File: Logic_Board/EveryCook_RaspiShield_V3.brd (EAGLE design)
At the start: 96.2 x 61.4 mm, 95 parts, among them IC1 TLP281-4, IC2 TLP281-4, J1 6P-2.54mm, J4 6P-2.54mm, J5 JUMPERSMD, Q2 IRLZ44N, U1 AD7794BRUZ, U2 PCA9685PW, U4 78M05, U7 CJ1117-3.3

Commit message: Schematic of logic board finished, only audio amp missing. Board ripped up for redraw
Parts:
- removed C4: 100uF/16V, Discrete:ELECTRO-SMD-C-6MM
- removed C8: 0.1uF, Discrete:0603
- removed D3: M7, Discrete:D2010
- removed IC1: TLP281-4, IC:SO16
- removed J1: 6P-2.54mm, Connector:6P-2.54-80/40MIL
- removed J14: (no value), Connector:2P-5.0
- removed J4: 6P-2.54mm, Connector:6P-2.54-65/35MIL
- removed J5: JUMPERSMD, Discrete:2P-JUMPER
- removed L2: 47uH, Discrete:0630
- removed R1, R10, R11, R12, R13, R18, R19, R20, R21, R26, R27, R28, R29, R6, R7, R8, R9: 1k, Discrete:0603
- removed R14: 51k, Discrete:0603
- removed R15, R22, R23, R24, R25: 10k, Discrete:0603
- removed R16: 2k, Discrete:0603
- removed R5: 4.7k, Discrete:0603
- removed U$2: LM2596, IC:TO-263
- removed U13, U14, U15, U16, U17: (no value), Connector:RJ45-N
- removed U2: PCA9685PW, wia:SOP65P640X110-28N
- added BUT1, BUT2, BUT3, C_CLOSE, C_LOCK, FAN, I2C, P_LOCK, THSTAT_POT: (no value), pinhead:1X02
- added C14: 22pF, Discrete:0603
- added C15: 0.1uF, Discrete:0603
- added DISPLAY, POWR_BRD: (no value), pinhead:2X06
- added Q1: 8 MHz, crystal:HC49UP
- added Q3: BSP372, infineon:PG-SOT-223
- added R3, R40, R45, R46: 10k, Discrete:0603
- added R39, R4, R44, R47, R48: 1k, Discrete:0603
- added T2: (no value), zetex:SM8
- added VALVE+PROXSW: (no value), pinhead:1X04
- added X1, X2, X3, X4, X5: MINI-USB_4P-85-32006-601-1, con-cypressindustries:85-32006-601-1
- C3: value 220uF/35V -> 22pF; device Discrete:ELECTRO-SMD-G-10MM -> Discrete:0603
- IC2: value TLP281-4 -> ATMEGA644A; device IC:SO16 -> atmel:TQFP44
- Q2: value IRLZ44N -> BSP372; device Discrete:D2PAK -> infineon:PG-SOT-223
- moved Q2 151.8 mm to (-64.8, -18.5), turned to 0 degrees
- moved C3 106.3 mm to (2.29, 80.1), turned to 0 degrees
- moved IC2 55.8 mm to (58.9, 71.8), turned to 0 degrees
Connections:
- removed net +24V: C2.+, C3.+, J2.2, U$2.1, U4.1
- removed net 3V3: C10.2, C17.2, C18.2, C6.+, C9.2, IC1.10, IC1.12, IC1.14, IC1.16, R26.2, R27.2, R28.2, R29.2, U1.22, U16.2, U16.6, U16.8, U17.10, U17.9, U2.28, U7.2, U7.4
- removed net BUTTON: IC2.11, IC2.13, IC2.15, IC2.9, J4.2
- removed net CS: U$1.24, U1.3
- removed net D5V: C1.+, C4.+, C8.2, J5.2, L2.P$2, U$2.4, U15.6, U7.3
- removed net GPIO1: R41.2, U$1.11, U16.1
- removed net GPIO2: R42.2, U$1.13, U16.3
- removed net KEY1: IC2.16, R5.1
- removed net KEY1S: IC2.2, U$1.12
- removed net KEY2: IC2.14, R14.1
- removed net KEY2S: IC2.4, U$1.16
- removed net KEY3: IC2.12, R15.1
- removed net KEY3S: IC2.6, U$1.18
- removed net KEY4: IC2.10, R16.1
- removed net KEY4S: IC2.8, U$1.22
- removed net LED: IC1.2, J4.3
- removed net LED-1: R6.2, U17.1
- removed net LED-2: R7.2, U17.2
- removed net LED-3: R8.2, U17.3
- removed net LED-4: R9.2, U17.4
- removed net LED-5: R10.2, U17.5
- removed net LED-6: R11.2, U17.6
- removed net LED-7: R12.2, U17.7
- removed net LED-8: R13.1, U17.8
- removed net LED1: IC1.4, J4.4
- removed net LED1S: IC1.13, R23.2, U$1.8
- removed net LED2: IC1.6, J4.5
- removed net LED2S: IC1.11, R24.2, U$1.10
- removed net LED3: IC1.8, J4.6
- removed net LED3S: IC1.9, R25.2, U$1.26
- removed net LEDS: IC1.15, R22.2, U$1.7
- removed net MVCC: J14.1, J3.1
- removed net N$13: R1.2, U2.6
- removed net N$14: J1.2, U2.18
- removed net N$20: IC1.1, R18.1
- removed net N$21: IC1.3, R19.1
- removed net N$22: IC1.5, R20.1
- removed net N$23: IC1.7, R21.1
- removed net N$25: R6.1, U2.8
- removed net N$26: R7.1, U2.9
- removed net N$27: R8.1, U2.10
- removed net N$28: R9.1, U2.11
- removed net N$29: R10.1, U2.12
- removed net N$3: Q2.1, R1.1
- removed net N$30: R11.1, U2.13
- removed net N$31: R12.1, U2.15
- removed net N$32: R13.2, U2.16
- removed net N$33: J1.3, U2.19
- removed net N$34: J1.4, U2.20
- removed net N$35: J1.5, U2.21
- removed net N$36: J1.6, U2.22
- removed net N$4: J1.1, U2.17
- removed net N$67: IC2.1, R26.1
- removed net N$68: IC2.3, R27.1
- removed net N$69: IC2.5, R28.1
- removed net N$70: IC2.7, R29.1
- removed net N$91: U15.7
- removed net SCL: U$1.5, U2.26
- removed net SDA: U$1.3, U2.27
- removed net SERVO_SIG: U15.8, U2.7
- new net +12V: C2.+, FAN.1, J3.1, U4.1, VALVE+PROXSW.1
- new net +3V3: C10.2, C15.2, C17.2, C18.2, C6.+, C9.2, IC2.38, IC2.5, POWR_BRD.4, R3.2, R45.1, U1.22, U7.2
- new net +5V: C1.+, J2.2, R46.2, T2.1, U7.3
- new net AVCC: IC2.27
- new net DAEMON_RST_LINE: IC2.19, R44.1
- new net FAN_PWM: Q2.1, R4.1
- new net IH_OFF: IC2.11, POWR_BRD.9
- new net IH_ON: POWR_BRD.5
- new net IH_PWR: IC2.15, POWR_BRD.1
- new net IH_RUN: IC2.12, POWR_BRD.7
- new net IH_THERMISTOR: IC2.36, POWR_BRD.2, R40.2
- new net MOT_PWM: IC2.14, POWR_BRD.3
- new net N$10: IC2.16, R4.2
- new net N$11: DISPLAY.12, IC2.21
- new net N$12: I2C.2, U$1.3
- new net N$15: DISPLAY.11, IC2.22
- new net N$16: DISPLAY.10, IC2.23
- new net N$17: DISPLAY.9, IC2.24
- new net N$18: DISPLAY.8, IC2.25
- new net N$19: DISPLAY.7, IC2.26
- new net N$37: DISPLAY.6, IC2.40
- new net N$38: DISPLAY.5, IC2.41
- new net N$39: DISPLAY.4, IC2.42
- new net N$41: DISPLAY.3, IC2.43
- new net N$43: DISPLAY.1, IC2.44
- new net N$49: DISPLAY.2, IC2.37
- new net N$50: I2C.1, U$1.5
- new net N$51: FAN.2, Q2.2
- new net N$52: IC2.9, U$1.8
- new net N$54: IC2.10, U$1.10
- new net N$55: IC2.2, U$1.16
- new net N$56: IC2.1, U$1.12
- new net N$59: C_CLOSE.1, IC2.30
- new net N$6: IC2.4, R3.1
- new net N$60: C_LOCK.1, IC2.31
- new net N$61: IC2.32, P_LOCK.1
- new net N$62: BUT2.1
- new net N$63: BUT3.1
- new net N$64: R39.2
- new net N$66: BUT1.1, R39.1, R44.2, R45.2
- new net N$7: C14.1, IC2.8, Q1.1
- new net N$71: R47.2, T2.4
- new net N$72: R46.1, T2.2, T2.5
- new net N$77: Q3.2, VALVE+PROXSW.2
- new net N$8: IC2.3, U$1.18
- new net PROX_SWI: IC2.35, VALVE+PROXSW.3
- new net RPI_RST: IC2.20, R47.1
- new net SAFETY_CHAIN: IC2.33
- new net VALVE_OPEN: Q3.1, R48.1
- net GND: now also BUT1.2, BUT2.2, BUT3.2, C14.2, C15.1, C3.2, C_CLOSE.2, C_LOCK.2, IC2.39, IC2.6, P_LOCK.2, Q2.3, Q3.3, R40.1, T2.3, THSTAT_POT.2, U1.3, VALVE+PROXSW.4, X1.4, X2.4, X3.4, X4.4, X5.4; no longer C3.-, C4.-, C8.1, D3.+, R22.1, R23.1, R24.1, R25.1, U$2.3, U$2.5, U13.3, U13.4, U14.3, U14.4, U15.3, U15.4, U16.5, U2.1, U2.14, U2.2, U2.23, U2.24, U2.25, U2.3, U2.4, U2.5, U4.3
- net GPIO3: no longer U$1.15, U16.7
- net L5V: now also X1.1, X2.1, X3.1, X4.1, X5.1; no longer U13.5, U13.6, U14.5, U14.6, U15.5
- net LOADCELL1_SIG+: now also X2.2; no longer U13.7
- net LOADCELL1_SIG-: now also X2.3; no longer U13.8
- net LOADCELL2_SIG+: now also X1.2; no longer U13.1
- net LOADCELL2_SIG-: now also X1.3; no longer U13.2
- net LOADCELL3_SIG+: now also X4.2; no longer U14.7
- net LOADCELL3_SIG-: now also X4.3; no longer U14.8
- net LOADCELL4_SIG+: now also X3.2; no longer U14.1
- net LOADCELL4_SIG-: now also X3.3; no longer U14.2
- net N$2: now also C3.1, IC2.7, Q1.2; no longer J14.2, Q2.2
- net N$58: now also T2.8; no longer J5.1
- net N$65: now also IC2.34, R48.2; no longer D3.-, L2.P$1, U$2.2
- net PGND: now also IC2.18, IC2.28; no longer Q2.3, U13.10, U13.9, U14.10, U14.9, U15.10, U15.9, U16.10, U16.9
- net PRESS_SIG+: now also X5.2; no longer U15.1
- net PRESS_SIG-: now also X5.3; no longer U15.2
- net TEMPER_SIG+: now also THSTAT_POT.1; no longer U16.4
- net VCC: now also IC2.17; no longer J4.1, R14.2, R15.2, R16.2, R18.2, R19.2, R20.2, R21.2, R5.2
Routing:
- net 3V3: track 184.8 -> 0.00 mm, vias 6 -> 0
- net PGND: track 169.9 -> 0.00 mm, vias 1 -> 0
- net L5V: track 160.6 -> 9.59 mm, vias 3 -> 0
- net D5V: track 102.3 -> 0.00 mm, vias 1 -> 0
- net LED-1: track 82.3 -> 0.00 mm, vias 2 -> 0
- net +24V: track 80.5 -> 0.00 mm
- net GPIO3: track 74.7 -> 0.00 mm, vias 1 -> 0
- net GPIO2: track 73.9 -> 0.00 mm, vias 1 -> 0
- net GPIO1: track 72.4 -> 0.00 mm, vias 1 -> 0
- net LED-8: track 70.5 -> 0.00 mm, vias 1 -> 0
- net LED-7: track 70.4 -> 0.00 mm, vias 1 -> 0
- net SERVO_SIG: track 66.9 -> 0.00 mm, vias 4 -> 0
- net LED-5: track 63.3 -> 0.00 mm, vias 2 -> 0
- net LED-2: track 59.3 -> 0.00 mm, vias 2 -> 0
- net LED-4: track 58.1 -> 0.00 mm, vias 1 -> 0
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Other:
- board text removed: "Total Cost: around 60RMB"

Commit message: Logic board all routed...
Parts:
- removed R41, R42, R43: 10k, Discrete:0603
- removed THSTAT_POT: (no value), pinhead:1X02
- removed U$1: RASPBERRY-PI, RaspberryPi:RASPBERRY-PI
- removed X1, X2, X3, X4, X5: MINI-USB_4P-85-32006-601-1, con-cypressindustries:85-32006-601-1
- added AIN_GND, AIN_SIG: (no value), wirepad:2,15/1,0
- added C16, C8: 10uF, Discrete:0603
- added C38: 100uF/25V, Discrete:ELECTRO-SMD-B-4.8MM
- added C4: 220pF, Discrete:0603
- added IC1: LM386MM-1, linear:MMSOP08
- added LC1, LC2, LC3, LC4, PRESS: MINI-USB_4P-85-32006-601-1, con-cypressindustries:85-32006-601-1
- added R1, R5: 5k, Discrete:0603
- added R6, R7: 10k, Discrete:0603
- added RASPI_CONNECTOR_(TOP): (no value), pinhead:2X13
- added SP1: AL23P, buzzer:AL23P
- added TEMP: (no value), pinhead:1X02
- R3: value 10k -> 22k
- T2: value (none) -> ZDT6790
- moved VALVE+PROXSW 359.0 mm to (89.5, 78.3)
- moved R48 320.6 mm to (66.2, 49.7), turned to 180 degrees
- moved Q3 317.5 mm to (76.7, 47.1), turned to 180 degrees
- moved R46 232.9 mm to (90.2, 52.2)
- moved T2 228.2 mm to (94.8, 48.0), turned to 270 degrees
- moved R47 227.3 mm to (90.5, 41.5), turned to 90 degrees
- moved R45 225.9 mm to (92.3, 66.2), turned to 90 degrees
- moved R39 223.7 mm to (94.4, 66.2), turned to 270 degrees
- moved R44 223.1 mm to (90.9, 66.2), turned to 90 degrees
- moved BUT1 215.6 mm to (94.4, 70.5), turned to 90 degrees
- moved BUT2 215.1 mm to (88.4, 70.5), turned to 90 degrees
- moved BUT3 215.1 mm to (82.7, 70.5), turned to 90 degrees
- moved P_LOCK 203.3 mm to (75.9, 77.3), turned to 90 degrees
- moved C_LOCK 203.1 mm to (81.3, 77.3), turned to 90 degrees
- moved C_CLOSE 183.8 mm to (70.2, 77.2), turned to 90 degrees
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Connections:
- removed net AVCC: IC2.27
- removed net GPIO3: R43.2
- removed net N$40: U$1.19, U1.24
- removed net VCC: IC2.17
- new net MOSI: RASPI_CONNECTOR_(TOP).19, U1.24
- new net N$14: IC1.3, R1.2, R5.1
- new net N$22: C16.1, C38.+, IC1.5
- new net N$23: C38.-, SP1.1
- new net N$27: AIN_SIG.1, C4.2
- new net N$3: C4.1, R5.2
- net +3V3: now also IC2.17, IC2.27, R6.1, R7.1
- net +5V: now also C16.2, IC1.6
- net GND: now also AIN_GND.1, C8.1, IC1.2, IC1.4, IC2.18, IC2.28, LC1.4, LC2.4, LC3.4, LC4.4, PRESS.4, R1.1, RASPI_CONNECTOR_(TOP).6, SP1.2, TEMP.2; no longer R41.1, R42.1, R43.1, THSTAT_POT.2, U$1.6, X1.4, X2.4, X3.4, X4.4, X5.4
- net IH_ON: now also IC2.13
- net L5V: now also LC1.1, LC2.1, LC3.1, LC4.1, PRESS.1; no longer X1.1, X2.1, X3.1, X4.1, X5.1
- net LOADCELL1_SIG+: now also LC1.2; no longer X2.2
- net LOADCELL1_SIG-: now also LC1.3; no longer X2.3
- net LOADCELL2_SIG+: now also LC2.2; no longer X1.2
- net LOADCELL2_SIG-: now also LC2.3; no longer X1.3
- net LOADCELL3_SIG+: now also LC3.2; no longer X4.2
- net LOADCELL3_SIG-: now also LC3.3; no longer X4.3
- net LOADCELL4_SIG+: now also LC4.2; no longer X3.2
- net LOADCELL4_SIG-: now also LC4.3; no longer X3.3
- net MISO: now also RASPI_CONNECTOR_(TOP).21; no longer U$1.21
- net N$12: now also RASPI_CONNECTOR_(TOP).3; no longer U$1.3
- net N$50: now also RASPI_CONNECTOR_(TOP).5; no longer U$1.5
- net N$52: now also RASPI_CONNECTOR_(TOP).8; no longer U$1.8
- net N$54: now also RASPI_CONNECTOR_(TOP).10; no longer U$1.10
- net N$55: now also RASPI_CONNECTOR_(TOP).16; no longer U$1.16
- net N$56: now also RASPI_CONNECTOR_(TOP).12; no longer U$1.12
- net N$58: now also RASPI_CONNECTOR_(TOP).2; no longer U$1.2
- net N$6: now also C8.2, RASPI_CONNECTOR_(TOP).11
- net N$62: now also R7.2, RASPI_CONNECTOR_(TOP).24
- net N$63: now also R6.2, RASPI_CONNECTOR_(TOP).26
- net N$64: now also RASPI_CONNECTOR_(TOP).22
- net N$8: now also RASPI_CONNECTOR_(TOP).18; no longer U$1.18
- net PGND: no longer IC2.18, IC2.28
- net PRESS_SIG+: now also PRESS.2; no longer X5.2
- net PRESS_SIG-: now also PRESS.3; no longer X5.3
- net SAFETY_CHAIN: now also POWR_BRD.11
- net SCLK: now also RASPI_CONNECTOR_(TOP).23; no longer U$1.23
- net TEMPER_SIG+: now also TEMP.1; no longer THSTAT_POT.1
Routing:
- net GND: track 11.2 -> 691.4 mm, vias 0 -> 11
- net +3V3: track 11.7 -> 271.7 mm, vias 0 -> 21
- net +5V: track 1.91 -> 187.2 mm, vias 0 -> 4
- net L5V: track 9.59 -> 186.9 mm, vias 0 -> 9
- net PGND: track 0.00 -> 152.4 mm
- net +12V: track 0.00 -> 142.3 mm
- net N$54: track 0.00 -> 84.0 mm, vias 0 -> 8
- net N$55: track 0.00 -> 77.7 mm, vias 0 -> 6
- net N$6: track 0.00 -> 77.1 mm, vias 0 -> 3
- net N$11: track 0.00 -> 76.2 mm, vias 0 -> 6
- net DAEMON_RST_LINE: track 0.00 -> 75.2 mm, vias 0 -> 4
- net IH_PWR: track 0.00 -> 73.3 mm, vias 0 -> 4
- net N$56: track 0.00 -> 71.7 mm, vias 0 -> 4
- net IH_OFF: track 0.00 -> 66.4 mm, vias 0 -> 3
- net IH_ON: track 0.00 -> 65.7 mm, vias 0 -> 4
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- added copper zone on layer 16, net N$21
- added copper zone on layer 1, net N$28
- removed copper zone on layer 1, net GND
- removed copper zone on layer 16, net GND
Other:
- board size 96.2 x 61.4 mm -> 103.1 x 86.4 mm
- board text added: "0V"
- board text added: "12V"
- board text added: "EveryCook.org/opensource"
- board text added: "connect cable with 3.5mm 90° angle jack"
- board text added: "pGND"
- board text added: "speaker (bottom side)"
- board text removed: "Change later probably to GPIO"
- board text removed: "EveryCook"
- board text removed: "Induction Conn"

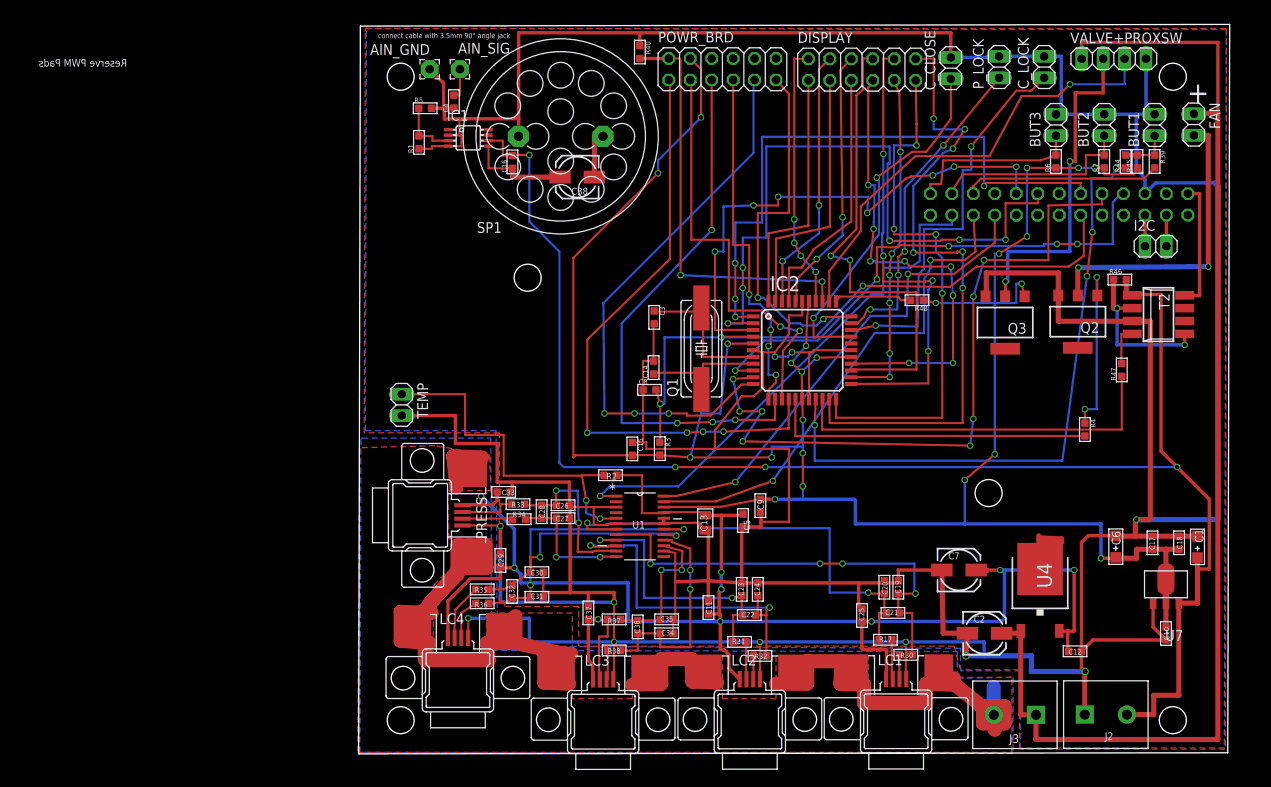
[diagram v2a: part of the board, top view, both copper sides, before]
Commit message: changed all 0606 to 0805 package for R and C.
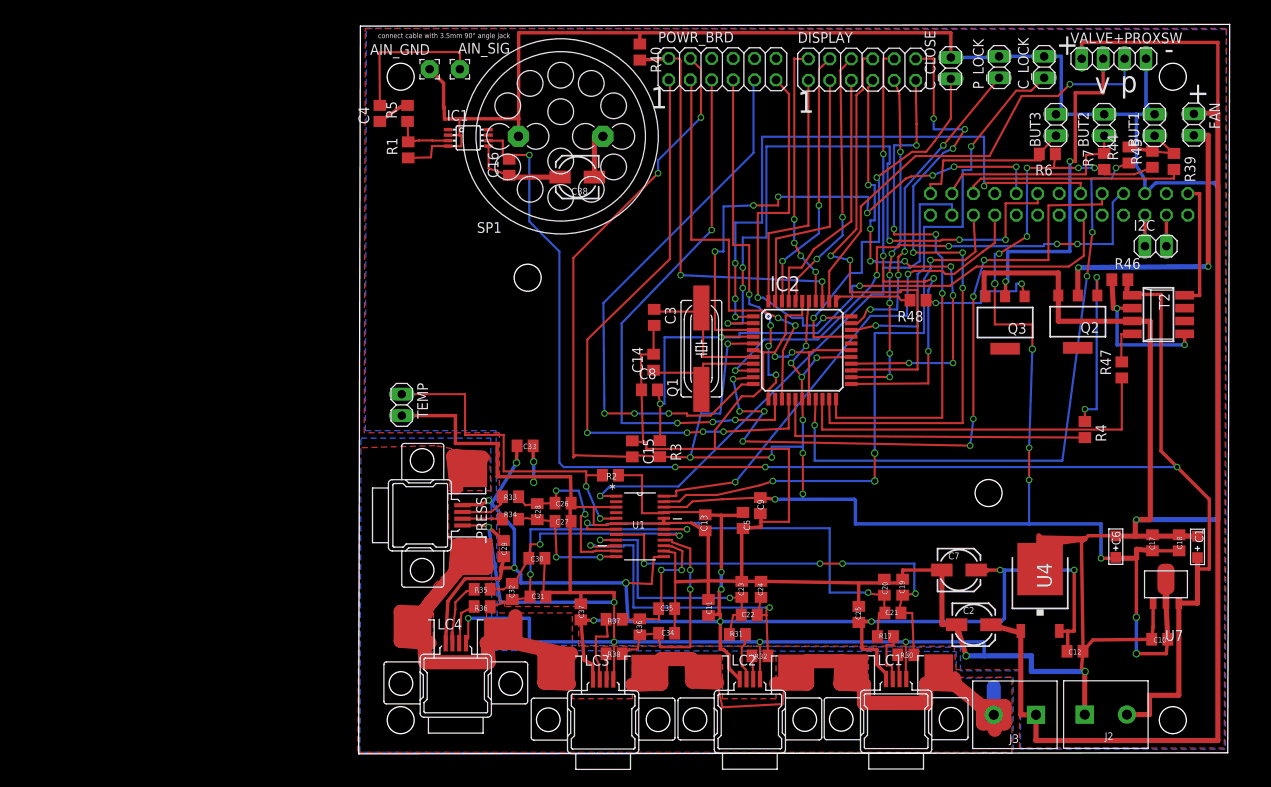
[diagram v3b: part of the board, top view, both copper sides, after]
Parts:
- C10, C11, C12, C14, C15, C16, C17, C18, C19, C20, C21, C22, C23, C24, C25, C26, C27, C28, C29, C3, C30, C31, C32, C33, C34, C35, C36, C37, C4, C5, C9: device Discrete:0603 -> rcl:C0805
- C13: device Discrete:0805 -> rcl:C0805
- C8: value 10uF -> 100nF; device Discrete:0603 -> rcl:C0805
- R1, R17, R3, R30, R31, R32, R33, R34, R35, R36, R37, R38, R39, R4, R40, R44, R45, R46, R47, R48, R5, R6, R7: device Discrete:0603 -> rcl:R0805
- R2: value 22k -> 2.2k; device Discrete:0603 -> rcl:R0805
- moved C4 8.87 mm to (2.62, 71.9)
- moved C33 6.02 mm to (19.8, 32.5)
- moved R39 2.29 mm to (96.6, 66.2)
- moved R5 2.17 mm to (5.89, 71.9), turned to 90 degrees
- moved R45 1.80 mm to (94.1, 66.4)
- moved C30 1.65 mm to (21.2, 19.2)
- moved C2 1.63 mm to (72.9, 11.3)
- moved R1 1.55 mm to (5.97, 67.5)
- moved C29 1.45 mm to (17.3, 20.3)
- moved R6 1.35 mm to (81.7, 67.1), turned to 180 degrees
- moved C35 1.27 mm to (36.6, 13.2)
- moved R33 1.26 mm to (18.1, 26.5)
- moved R34 1.02 mm to (18.1, 23.8)
- moved C10 1.01 mm to (95.0, 9.58), turned to 0 degrees
- moved R31 0.92 mm to (45.0, 10.2)
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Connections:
- net +3V3: now also U7.4
- net GND: now also U4.3
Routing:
- net GND: track 691.4 -> 718.0 mm, vias 11 -> 13
- net +3V3: track 271.7 -> 290.1 mm, vias 21 -> 25
- net L5V: track 186.9 -> 204.0 mm, vias 9 -> 11
- net N$27: track 3.78 -> 17.8 mm
- net PGND: track 152.4 -> 164.9 mm
- net MISO: track 59.3 -> 67.7 mm, vias 2 -> 4
- net N$26: track 5.21 -> 0.00 mm
- net N$64: track 23.2 -> 26.1 mm
- net N$66: track 5.72 -> 8.50 mm
- net SCLK: track 62.3 -> 64.8 mm
- net N$59: track 42.6 -> 44.9 mm
- net N$2: track 17.3 -> 19.3 mm
- net LOADCELL1_SIG+: track 4.76 -> 6.60 mm
- net +12V: track 142.3 -> 143.9 mm
- net LOADCELL4_SIG+: track 6.08 -> 7.66 mm
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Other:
- board text added: "1"
- board text added: "p"
- board text added: "v"
- board text removed: "2013-04-26 V0.3"
- board text removed: "EveryCook.org"
- board text removed: "RaspberryPi Control Shield"
- board text removed: "Reserve PWM Pads"
- board text removed: "by Tobe@NOA-Labs.com"
